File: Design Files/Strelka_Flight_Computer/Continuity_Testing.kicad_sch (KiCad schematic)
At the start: 0 parts

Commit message: Added boost converter
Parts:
- added Q?: AP2300, Package_TO_SOT_SMD:SOT-23, symbol Transistor_FET:2N7002E
- added R? (x5): R_Small, symbol Device:R_Small
- added U?: LM321, Package_TO_SOT_SMD:SOT-23-5, symbol Amplifier_Operational:LM321
- added U?: LM334M, Package_SO:SOIC-8_3.9x4.9mm_P1.27mm, symbol Reference_Current:LM334M
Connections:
- new net: R?.1, R?.2, U?.1 (+)
- new net: R?.1, R?.2, U?.3 (-)
- new net: Q?.1 (G), R?.1
- new net +3V3: U?.2 (V-)
- new net CONT_TEST: R?.2
- new net E-match1+: R?.1, U?.2, U?.3, U?.6, U?.7
- new net E-match1-: Q?.3 (D), R?.1
- new net E-match1_Cont: R?.2, U?.4
- new net GND: Q?.2 (S), R?.2, U?.5 (V+)
- new net VDC: U?.4
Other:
- note added: "Battery voltage applied"

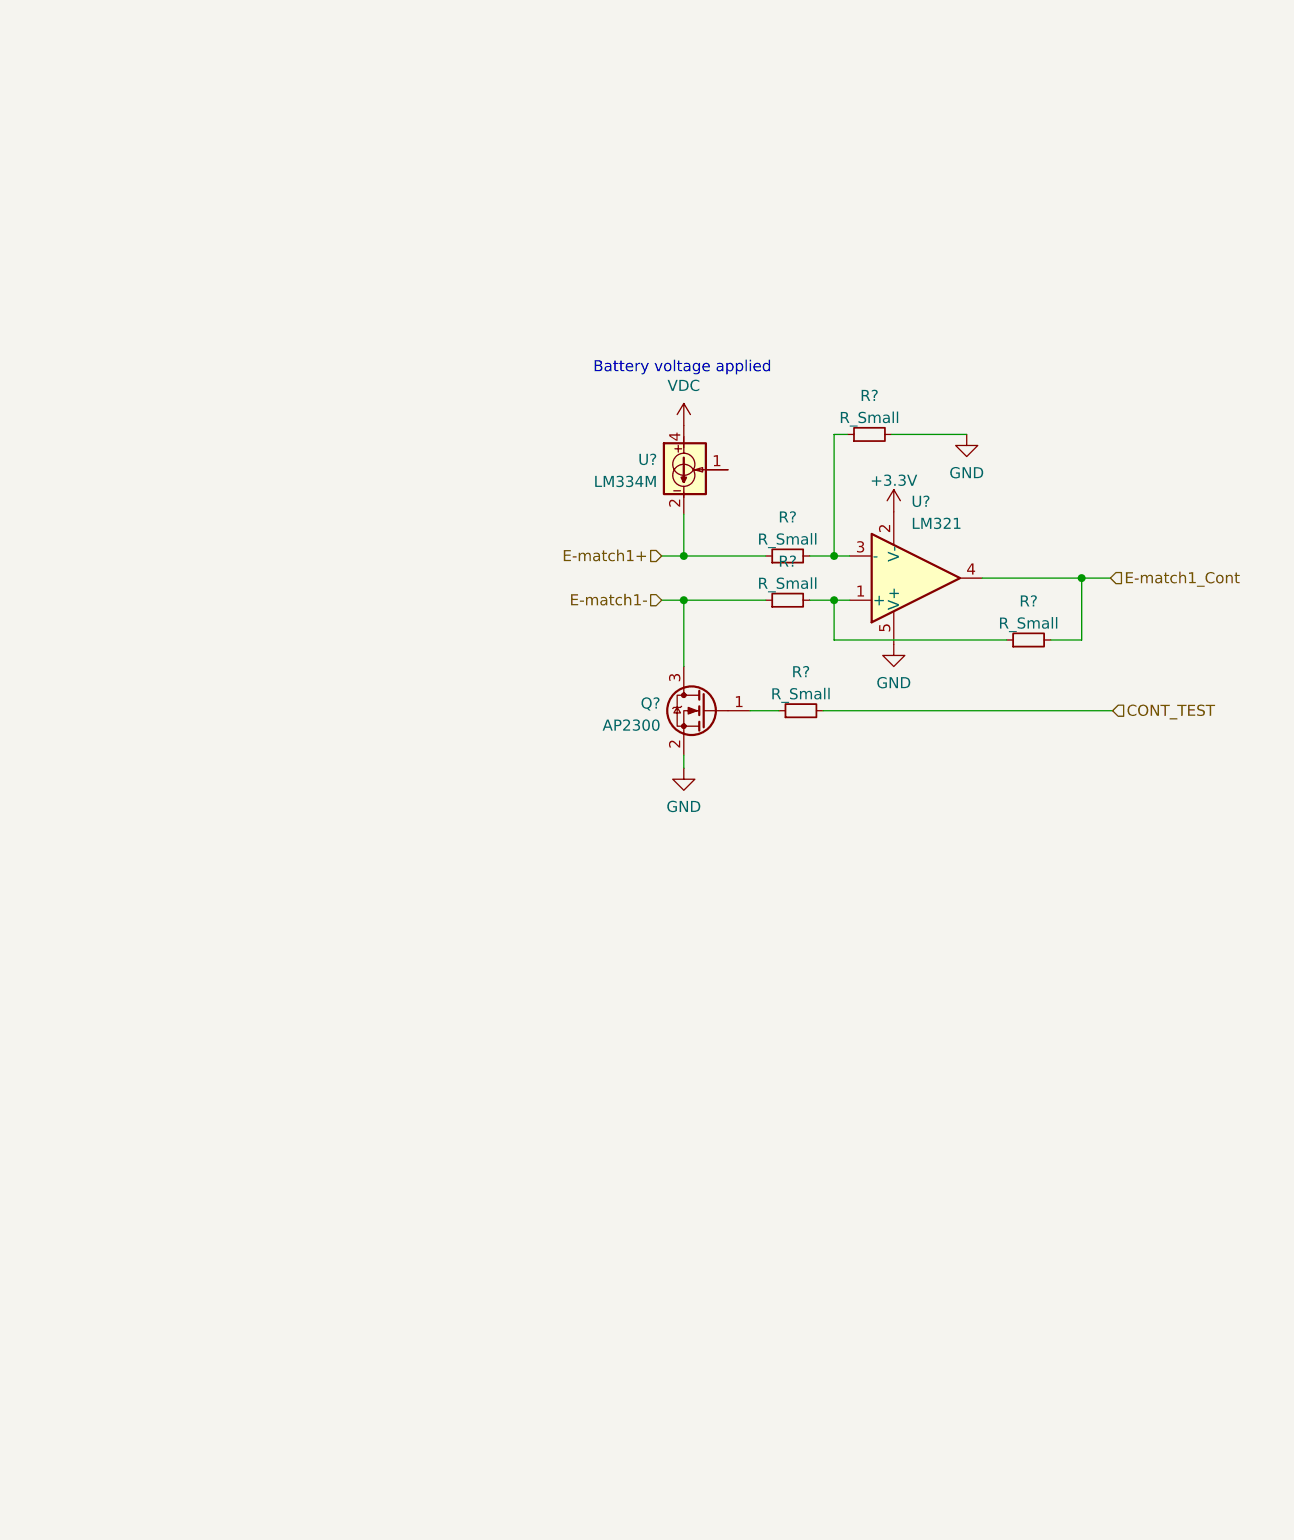
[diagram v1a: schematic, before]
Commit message: Added BMX055
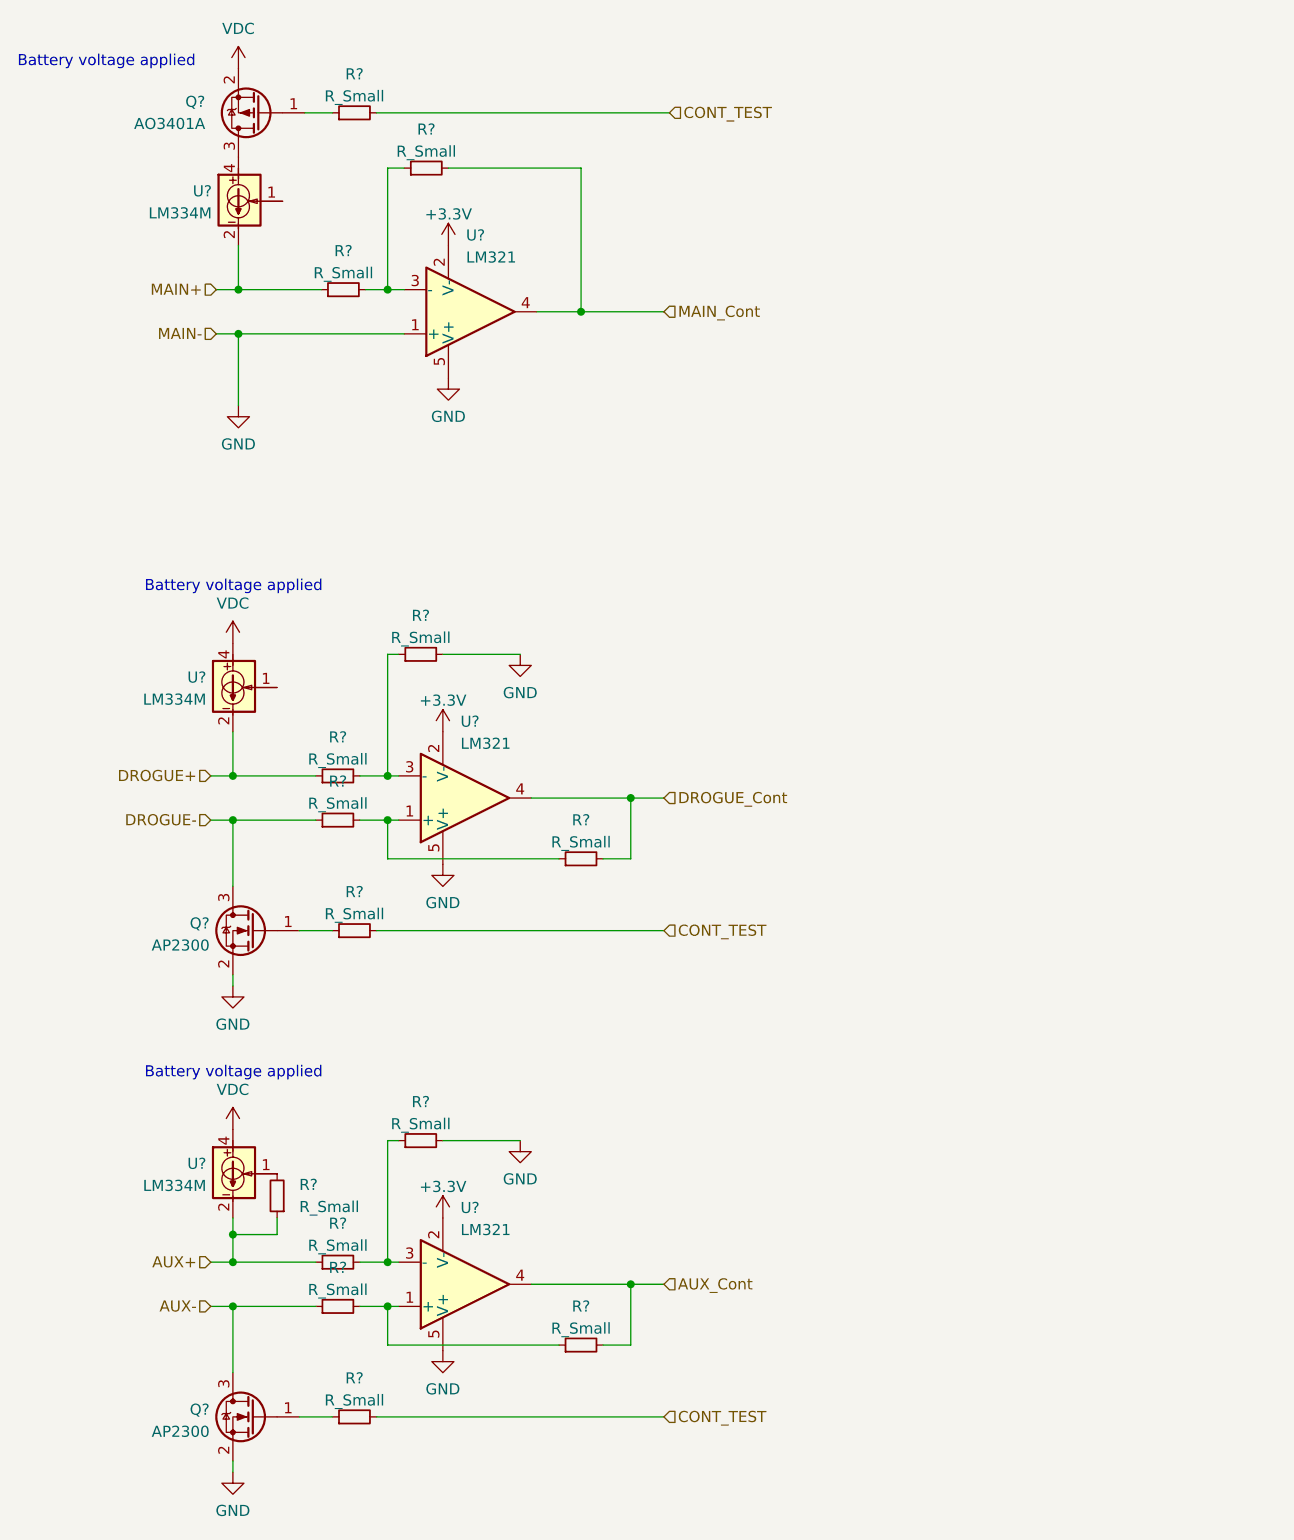
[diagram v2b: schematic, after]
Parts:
- removed Q?: AP2300, Package_TO_SOT_SMD:SOT-23, symbol Transistor_FET:2N7002E
- removed R? (x2): R_Small, symbol Device:R_Small
- added Q? (x2): AP2300, Package_TO_SOT_SMD:SOT-23, symbol Transistor_FET:2N7002E
- added Q?: AO3401A, Package_TO_SOT_SMD:SOT-23, symbol Transistor_FET:AO3401A
- added R? (x11): R_Small, symbol Device:R_Small
- added U? (x2): LM321, Package_TO_SOT_SMD:SOT-23-5, symbol Amplifier_Operational:LM321
- added U? (x2): LM334M, Package_SO:SOIC-8_3.9x4.9mm_P1.27mm, symbol Reference_Current:LM334M
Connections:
- net +3V3: now also U?.2 (V-), U?.2 (V-)
- net CONT_TEST: now also R?.2, R?.2
- net GND: now also U?.1 (+), Q?.2 (S), Q?.2 (S), R?.2, R?.2, U?.5 (V+), U?.5 (V+); no longer R?.2
- net VDC: now also Q?.2 (S), U?.4, U?.4; no longer U?.4
- net at R?.1: now also Q?.1 (G)
- net E-match1+ renamed MAIN+
- net E-match1_Cont renamed MAIN_Cont
- net MAIN_Cont: now also R?.2
- new net: R?.1, R?.2, U?.3 (-) (x2)
- new net: Q?.1 (G), R?.1 (x2)
- new net: R?.1, R?.2, U?.1 (+) (x2)
- new net: R?.2, U?.1
- new net: Q?.3 (D), U?.4
- new net AUX+: R?.1, R?.1, U?.2, U?.3, U?.6, U?.7
- new net AUX-: Q?.3 (D), R?.1
- new net AUX_Cont: R?.2, U?.4
- new net DROGUE+: R?.1, U?.2, U?.3, U?.6, U?.7
- new net DROGUE-: Q?.3 (D), R?.1
- new net DROGUE_Cont: R?.2, U?.4
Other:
- moved on the sheet: R?, U?

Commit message: Working SPICE sim for ematch continuity circuit
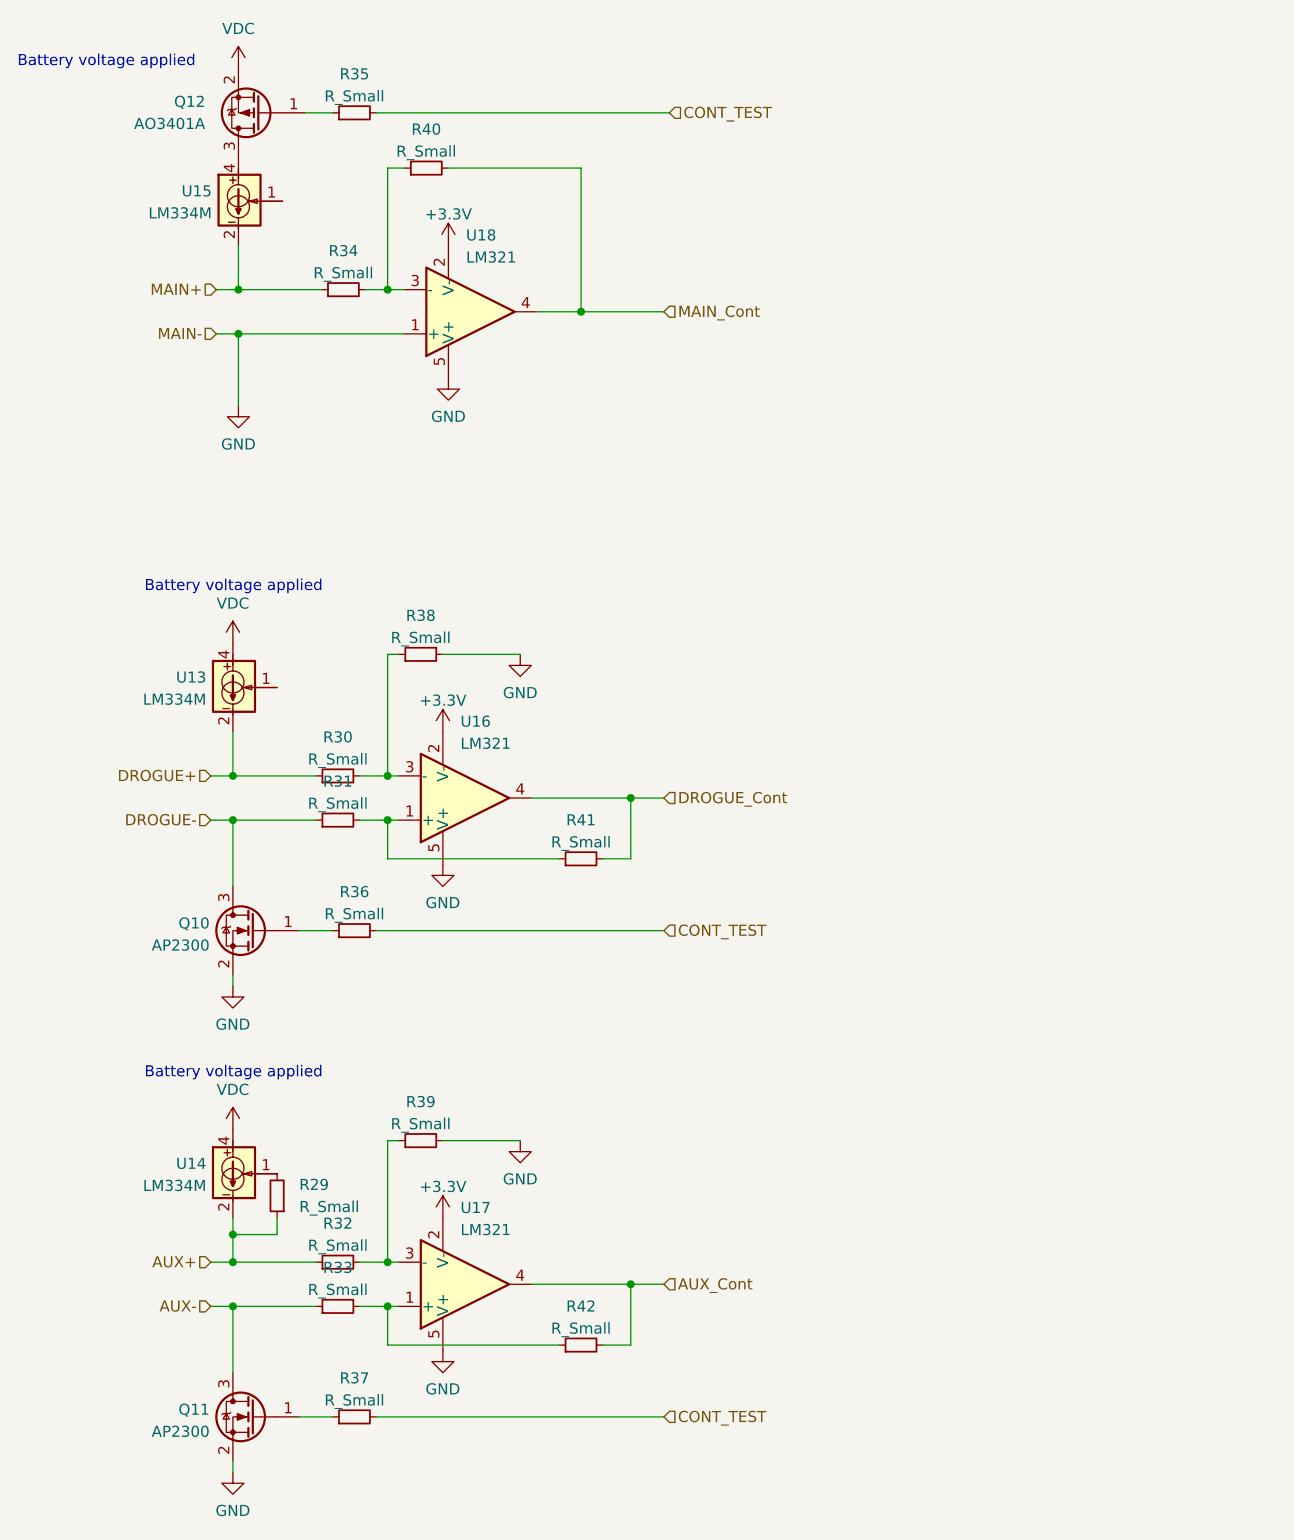
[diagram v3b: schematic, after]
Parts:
- gave numbers to parts that had none: 23
